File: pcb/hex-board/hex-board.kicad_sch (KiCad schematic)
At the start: 18 parts

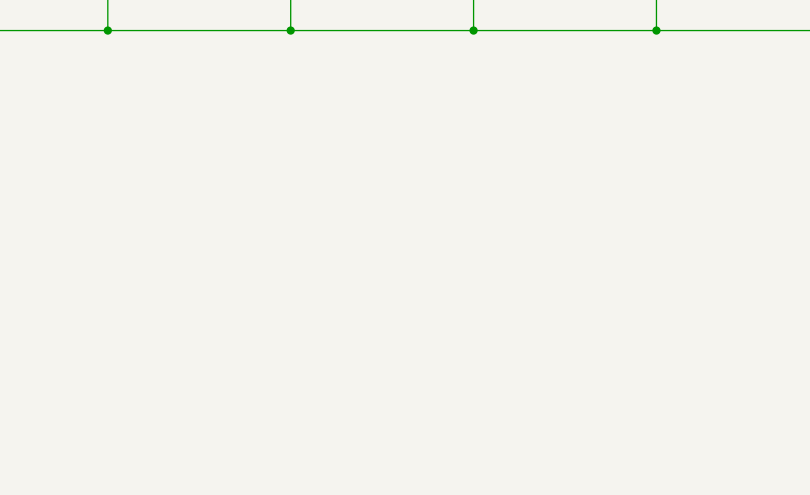
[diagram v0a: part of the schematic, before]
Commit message: Added JST connector to hex board
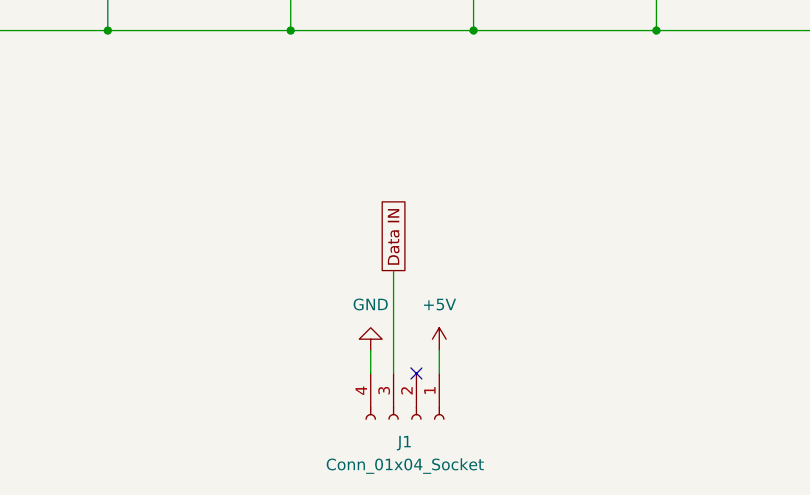
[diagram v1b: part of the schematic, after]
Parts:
- added J1: Conn_01x04_Socket, Connector_JST:JST_EH_S4B-EH_1x04_P2.50mm_Horizontal, symbol Connector:Conn_01x04_Socket
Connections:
- net +5V: now also J1.1 (Pin_1)
- net Data IN: now also J1.3 (Pin_3)
- net GND: now also J1.4 (Pin_4)
- no-connect marks 0 -> 1
